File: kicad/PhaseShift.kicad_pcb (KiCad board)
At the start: 2 copper layers, 66.4 x 128.6 mm, 54 parts

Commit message: Silk Screen
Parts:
- added G***: LOGO, omnicode-9001:OmniCode-9001, F.Cu at (203.9, 150.6)
- added G***: LOGO, omnicode-9001:OmniCode-9001, B.Cu at (203.9, 150.7)
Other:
- board text added: "OmniCode:9001 - 202507.01"
- board text added: "OmniCode:9001 - PhaseShift"
- board text added: "PhaseShift"

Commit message: changed screw sizes
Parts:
- H1, H2, H3, H4, H5: value MountingHole_3.2mm_Pad -> MountingHole_2.2mm_M2_Pad; footprint TB2086_MISC:MountingHole_3.2mm_Pad -> TB2086_MISC:MountingHole_2.2mm_M2_Pad
- moved LED1 0.41 mm to (185.4, 101.9)
- moved R1 0.41 mm to (185.4, 101.9)
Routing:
- net Net-(LED1-K): track 4.27 -> 2.13 mm
- net +5V: track 318.8 -> 318.1 mm
- net ROW13: track 159.0 -> 158.4 mm
- net Net-(L11-DIN): track 15.0 -> 14.4 mm
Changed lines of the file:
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@@
 		)
 	)
-	(footprint "TB2086_MISC:MountingHole_3.2mm_Pad"
+	(footprint "TB2086_MISC:MountingHole_2.2mm_M2_Pad"
 		(layer "F.Cu")
 		(at 214.025 142.3875)
-		(descr "Mounting Hole 3.2mm, no annular, M3")
-		(tags "mounting hole 3.2mm no annular m3")
+		(descr "Mounting Hole 2.2mm, M2")
+		(tags "mounting hole 2.2mm m2")
 		(property "Reference" "H5"
-			(at 0 -4.2 0)
+			(at 0 -3.2 0)
 			(layer "F.SilkS")
 			(hide yes)
@@
 			)
 		)
-		(property "Value" "MountingHole_3.2mm_Pad"
-			(at 0 4.2 0)
+		(property "Value" "MountingHole_2.2mm_M2_Pad"
+			(at 0 3.2 0)
 			(layer "F.Fab")
 			(effects
@@
 		(fp_circle
 			(center 0 0)
-			(end 3.2 0)
+			(end 2.2 0)
 			(stroke
 				(width 0.15)
@@
 		(fp_circle
 			(center 0 0)
-			(end 3.45 0)
+			(end 2.45 0)
 			(stroke
 				(width 0.05)
@@
 		(pad "1" thru_hole circle
 			(at 0 0)
-			(size 3.5 3.5)
-			(drill 3.2)
+			(size 4.4 4.4)
+			(drill 2.2)
 			(layers "*.Cu" "*.Mask")
 			(remove_unused_layers no)
 			(net 1 "GND")
-			(zone_connect 2)
 		)
 		(embedded_fonts no)
@@
 		)
 	)
-	(footprint "TB2086_MISC:MountingHole_3.2mm_Pad"
+	(footprint "TB2086_MISC:MountingHole_2.2mm_M2_Pad"
 		(layer "F.Cu")
 		(at 233.675 200.3)
-		(descr "Mounting Hole 3.2mm, no annular, M3")
-		(tags "mounting hole 3.2mm no annular m3")
+		(descr "Mounting Hole 2.2mm, M2")
+		(tags "mounting hole 2.2mm m2")
 		(property "Reference" "H3"
-			(at 0 -4.2 0)
+			(at 0 -3.2 0)
 			(layer "F.SilkS")
 			(hide yes)
@@
 			)
 		)
-		(property "Value" "MountingHole_3.2mm_Pad"
-			(at 0 4.2 0)
+		(property "Value" "MountingHole_2.2mm_M2_Pad"
+			(at 0 3.2 0)
 			(layer "F.Fab")
 			(effects
@@
 		(fp_circle
 			(center 0 0)
-			(end 3.2 0)
+			(end 2.2 0)
 			(stroke
 				(width 0.15)
@@
 		(fp_circle
 			(center 0 0)
-			(end 3.45 0)
+			(end 2.45 0)
 			(stroke
 				(width 0.05)
@@
 		(pad "1" thru_hole circle
 			(at 0 0)
-			(size 3.5 3.5)
-			(drill 3.2)
+			(size 4.4 4.4)
+			(drill 2.2)
 			(layers "*.Cu" "*.Mask")
 			(remove_unused_layers no)
 			(net 1 "GND")
-			(zone_connect 2)
 		)
 		(embedded_fonts no)
@@
 		)
 	)
-	(footprint "TB2086_MISC:MountingHole_3.2mm_Pad"
+	(footprint "TB2086_MISC:MountingHole_2.2mm_M2_Pad"
 		(layer "F.Cu")
 		(at 175.325 79.7125)
-		(descr "Mounting Hole 3.2mm, no annular, M3")
-		(tags "mounting hole 3.2mm no annular m3")
+		(descr "Mounting Hole 2.2mm, M2")
+		(tags "mounting hole 2.2mm m2")
 		(property "Reference" "H1"
-			(at 0 -4.2 0)
+			(at 0 -3.2 0)
 			(layer "F.SilkS")
 			(hide yes)
@@
 			)
 		)
-		(property "Value" "MountingHole_3.2mm_Pad"
-			(at 0 4.2 0)
+		(property "Value" "MountingHole_2.2mm_M2_Pad"
+			(at 0 3.2 0)
 			(layer "F.Fab")
 			(effects
@@
 		(fp_circle
 			(center 0 0)
-			(end 3.2 0)
+			(end 2.2 0)
 			(stroke
 				(width 0.15)
@@
 		(fp_circle
 			(center 0 0)
-			(end 3.45 0)
+			(end 2.45 0)
 			(stroke
 				(width 0.05)
@@
 		(pad "1" thru_hole circle
 			(at 0 0)
-			(size 3.5 3.5)
-			(drill 3.2)
+			(size 4.4 4.4)
+			(drill 2.2)
 			(layers "*.Cu" "*.Mask")
 			(remove_unused_layers no)
 			(net 1 "GND")
-			(zone_connect 2)
 		)
 		(embedded_fonts no)
@@
 		)
 	)
-	(footprint "TB2086_MISC:MountingHole_3.2mm_Pad"
+	(footprint "TB2086_MISC:MountingHole_2.2mm_M2_Pad"
 		(layer "F.Cu")
 		(at 233.675 79.7125)
-		(descr "Mounting Hole 3.2mm, no annular, M3")
-		(tags "mounting hole 3.2mm no annular m3")
+		(descr "Mounting Hole 2.2mm, M2")
+		(tags "mounting hole 2.2mm m2")
 		(property "Reference" "H2"
-			(at 0 -4.2 0)
+			(at 0 -3.2 0)
 			(layer "F.SilkS")
 			(hide yes)
@@
 			)
 		)
-		(property "Value" "MountingHole_3.2mm_Pad"
-			(at 0 4.2 0)
+		(property "Value" "MountingHole_2.2mm_M2_Pad"
+			(at 0 3.2 0)
 			(layer "F.Fab")
 			(effects
@@
 		(fp_circle
 			(center 0 0)
-			(end 3.2 0)
+			(end 2.2 0)
 			(stroke
 				(width 0.15)
@@
 		(fp_circle
 			(center 0 0)
-			(end 3.45 0)
+			(end 2.45 0)
 			(stroke
 				(width 0.05)
@@
 		(pad "1" thru_hole circle
 			(at 0 0)
-			(size 3.5 3.5)
-			(drill 3.2)
+			(size 4.4 4.4)
+			(drill 2.2)
 			(layers "*.Cu" "*.Mask")
 			(remove_unused_layers no)
 			(net 1 "GND")
-			(zone_connect 2)
 		)
 		(embedded_fonts no)
@@
 		)
 	)
-	(footprint "TB2086_MISC:MountingHole_3.2mm_Pad"
+	(footprint "TB2086_MISC:MountingHole_2.2mm_M2_Pad"
 		(layer "F.Cu")
 		(at 175.325 200.3)
-		(descr "Mounting Hole 3.2mm, no annular, M3")
-		(tags "mounting hole 3.2mm no annular m3")
+		(descr "Mounting Hole 2.2mm, M2")
+		(tags "mounting hole 2.2mm m2")
 		(property "Reference" "H4"
-			(at 0 -4.2 0)
+			(at 0 -3.2 0)
 			(layer "F.SilkS")
 			(hide yes)
@@
 			)
 		)
-		(property "Value" "MountingHole_3.2mm_Pad"
-			(at 0 4.2 0)
+		(property "Value" "MountingHole_2.2mm_M2_Pad"
+			(at 0 3.2 0)
 			(layer "F.Fab")
 			(effects
@@
 		(fp_circle
 			(center 0 0)
-			(end 3.2 0)
+			(end 2.2 0)
 			(stroke
 				(width 0.15)
@@
 		(fp_circle
 			(center 0 0)
-			(end 3.45 0)
+			(end 2.45 0)
 			(stroke
 				(width 0.05)
@@
 		(pad "1" thru_hole circle
 			(at 0 0)
-			(size 3.5 3.5)
-			(drill 3.2)
+			(size 4.4 4.4)
+			(drill 2.2)
 			(layers "*.Cu" "*.Mask")
 			(remove_unused_layers no)
 			(net 1 "GND")
-			(zone_connect 2)
 		)
 		(embedded_fonts no)
@@
 	(footprint "LED_SMD:LED_0603_1608Metric_Pad1.05x0.95mm_HandSolder"
 		(layer "F.Cu")
-		(at 185.45 101.5 180)
+		(at 185.45 101.90625 180)
 		(descr "LED SMD 0603 (1608 Metric), square (rectangular) end terminal, IPC-7351 nominal, (Body size source: http://www.tortai-tech.com/upload/download/2011102023233369053.pdf), generated with kicad-footprint-generator")
 		(tags "LED handsolder")
@@
 	(footprint "Resistor_SMD:R_0603_1608Metric"
 		(layer "B.Cu")
-		(at 185.45 101.5)
+		(at 185.45 101.90625)
 		(descr "Resistor SMD 0603 (1608 Metric), square (rectangular) end terminal, IPC-7351 nominal, (Body size source: IPC-SM-782 page 72, https://www.pcb-3d.com/wordpress/wp-content/uploads/ipc-sm-782a_amendment_1_and_2.pdf), generated with kicad-footprint-generator")
 		(tags "resistor")
@@
 			(net 1 "GND")
 			(pintype "passive")
+			(zone_connect 2)
 		)
 		(pad "2" smd roundrect
@@
 	)
 	(segment
-		(start 175.45 176.92)
-		(end 175.89 177.36)
-		(width 0.2)
-		(layer "B.Cu")
-		(net 4)
-	)
-	(segment
 		(start 202.775 122.6908)
 		(end 202.775 122.8125)
@@
 	)
 	(segment
-		(start 226.822 128.6325)
-		(end 226.3 128.6325)
-		(width 0.5)
-		(layer "B.Cu")
-		(net 24)
-	)
-	(segment
 		(start 201.75 184.0825)
 		(end 202.049 183.7835)
@@
 	)
 	(segment
-		(start 182.5658 107.7483)
-		(end 182.7 107.8825)
-		(width 0.5)
-		(layer "B.Cu")
-		(net 24)
-	)
-	(segment
 		(start 202.049 183.121426)
 		(end 202.600426 182.57)
@@
 	)
 	(segment
-		(start 201.1525 185.7825)
-		(end 201.75 185.7825)
-		(width 0.2)
-		(layer "B.Cu")
-		(net 34)
-	)
-	(segment
 		(start 188.2 184.0825)
 		(end 189.0425 183.24)
@@
 	)
 	(segment
-		(start 184.575 101.5)
-		(end 176.0475 92.9725)
+		(start 184.575 101.90625)
+		(end 176.0475 93.37875)
 		(width 0.2)
 		(layer "F.Cu")
@@
 	)
 	(segment
-		(start 185.0857 99.8667)
-		(end 186.325 101.106)
+		(start 187.62625 101.90625)
+		(end 187.73 102.01)
 		(width 0.2)
 		(layer "F.Cu")
@@
 	)
 	(segment
-		(start 186.325 101.106)
-		(end 186.325 101.5)
+		(start 186.73125 101.90625)
+		(end 187.62625 101.90625)
 		(width 0.2)
 		(layer "F.Cu")
@@
 	)
 	(via
-		(at 185.0857 99.8667)
+		(at 187.73 102.01)
 		(size 0.8)
 		(drill 0.4)
@@
 	)
 	(segment
-		(start 186.275 101.5)
-		(end 185.0857 100.3107)
+		(start 187.62625 101.90625)
+		(end 187.73 102.01)
 		(width 0.2)
 		(layer "B.Cu")
@@
 	)
 	(segment
-		(start 185.0857 100.3107)
-		(end 185.0857 99.8667)
+		(start 186.68125 101.90625)
+		(end 187.62625 101.90625)
 		(width 0.2)
 		(layer "B.Cu")
@@
 		(width 0.2)
 		(layer "B.Cu")
-		(net 43)
-	)
-	(segment
-		(start 175.45 147.4675)
-		(end 175.6425 147.66)
-		(width 0.2)
-		(layer "B.Cu")

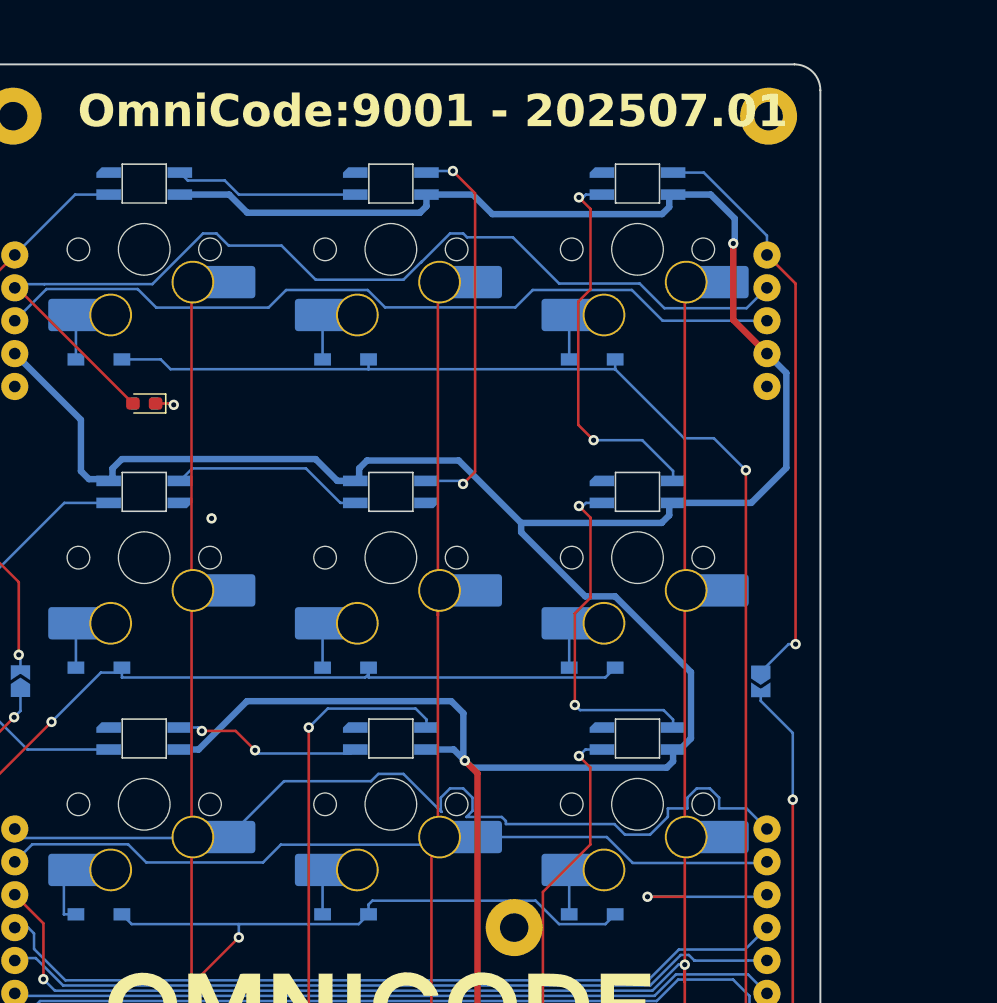
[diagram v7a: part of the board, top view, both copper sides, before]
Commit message: fixed positions for screw holes
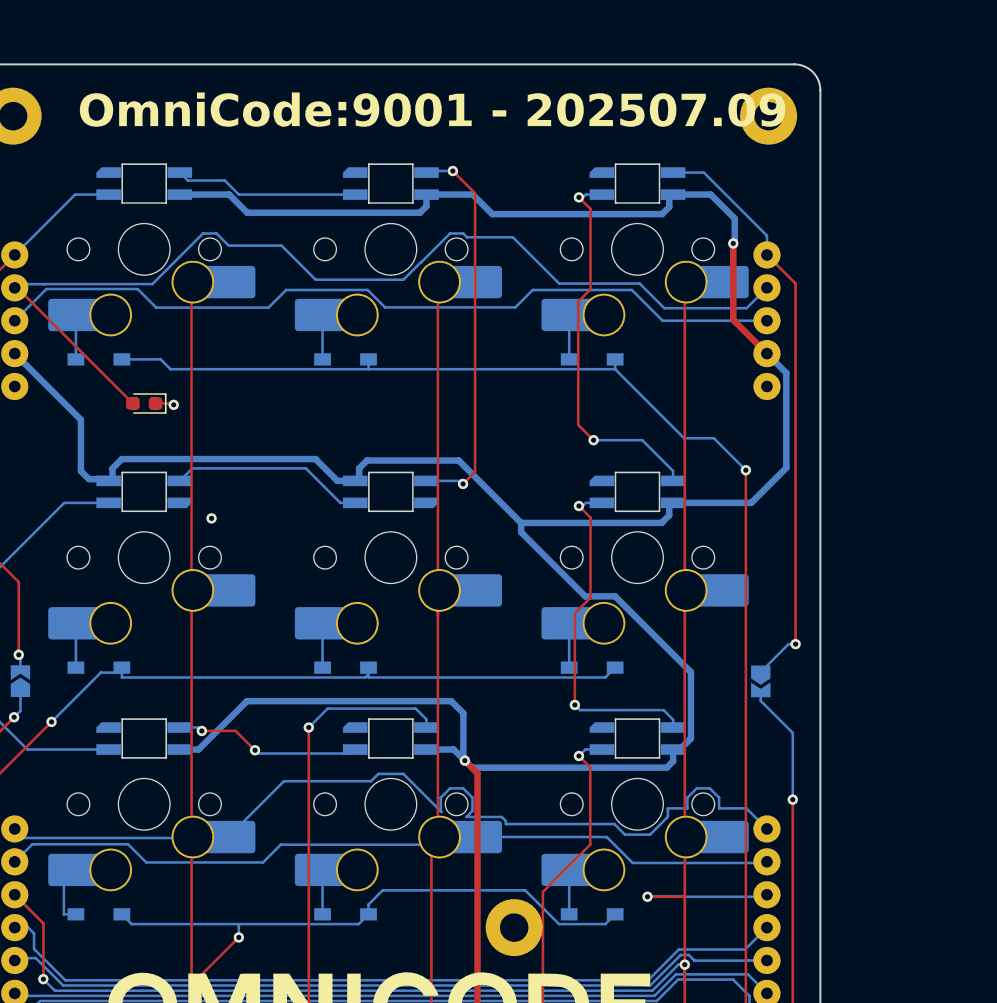
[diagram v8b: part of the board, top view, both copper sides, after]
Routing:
- net ROW14: track 137.1 -> 137.8 mm
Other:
- board text added: "OmniCode:9001 - 202507.09"
- board text removed: "OmniCode:9001 - 202507.01"
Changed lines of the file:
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@@
 		)
 	)
-	(gr_text "OmniCode:9001 - 202507.01"
+	(gr_text "OmniCode:9001 - 202507.09"
 		(at 180.31 80.79 0)
 		(layer "F.SilkS")
@@
 			(justify left bottom)
 		)
-		(render_cache "OmniCode:9001 - 202507.01" 0
+		(render_cache "OmniCode:9001 - 202507.09" 0
 			(polygon
 				(pts
@@
 			(polygon
 				(pts
-					(xy 225.536753 80.365) (xy 225.536753 80.091448) (xy 226.11744 80.091448) (xy 226.11744 78.066064)
-					(xy 225.561635 78.371978) (xy 225.495689 78.371978) (xy 225.495689 78.086519) (xy 226.213306 77.707637)
-					(xy 226.453427 77.707637) (xy 226.453427 80.091448) (xy 226.967405 80.091448) (xy 226.967405 80.365)
+					(xy 226.282498 77.690285) (xy 226.425442 77.724486) (xy 226.551128 77.779445) (xy 226.66219 77.855098)
+					(xy 226.760409 77.952796) (xy 226.858126 78.095255) (xy 226.930012 78.261304) (xy 226.975339 78.455318)
+					(xy 226.991372 78.682777) (xy 226.976305 78.919584) (xy 226.932019 79.141523) (xy 226.859086 79.350938)
+					(xy 226.757011 79.549821) (xy 226.624244 79.739738) (xy 226.367748 80.04051) (xy 226.163613 80.244987)
+					(xy 226.002646 80.374769) (xy 225.572626 80.374769) (xy 225.572626 80.259822) (xy 225.821129 80.10649)
+					(xy 226.046423 79.929154) (xy 226.250095 79.726915) (xy 226.433078 79.501853) (xy 226.551491 79.313449)
+					(xy 226.619207 79.155234) (xy 226.470613 79.26872) (xy 226.319551 79.345744) (xy 226.161845 79.392525)
+					(xy 226.011195 79.407568) (xy 225.846502 79.392584) (xy 225.703672 79.349598) (xy 225.578502 79.279674)
+					(xy 225.46806 79.181338) (xy 225.379604 79.062712) (xy 225.315583 78.927549) (xy 225.27577 78.772742)
+					(xy 225.261827 78.594239) (xy 225.262791 78.582332) (xy 225.602851 78.582332) (xy 225.613079 78.713774)
+					(xy 225.641635 78.822056) (xy 225.686516 78.911446) (xy 225.747412 78.98518) (xy 225.851072 79.06163)
+					(xy 225.972087 79.108044) (xy 226.115456 79.124246) (xy 226.25513 79.111059) (xy 226.387786 79.071734)
+					(xy 226.513861 79.010599) (xy 226.635235 78.930531) (xy 226.645921 78.784748) (xy 226.650195 78.630112)
+					(xy 226.639549 78.467882) (xy 226.609885 78.333438) (xy 226.563664 78.222094) (xy 226.50197 78.130025)
+					(xy 226.421724 78.051648) (xy 226.332041 77.996756) (xy 226.230958 77.963416) (xy 226.115456 77.95188)
+					(xy 226.003133 77.963094) (xy 225.905521 77.995406) (xy 225.819566 78.048461) (xy 225.743291 78.124071)
+					(xy 225.667736 78.245988) (xy 225.619992 78.39628) (xy 225.602851 78.582332) (xy 225.262791 78.582332)
+					(xy 225.276933 78.407706) (xy 225.320815 78.23966) (xy 225.392705 78.08678) (xy 225.493705 77.946537)
+					(xy 225.618567 77.830063) (xy 225.761698 77.747224) (xy 225.926727 77.696182) (xy 226.118967 77.678328)
 				)
 			)
 		)
 	)
-	(gr_text "OmniCode:9001 - 202507.01"
+	(gr_text "OmniCode:9001 - 202507.09"
 		(at 228.19 80.79 0)
 		(layer "B.SilkS")
@@
 			(justify left bottom mirror)
 		)
-		(render_cache "OmniCode:9001 - 202507.01" 0
+		(render_cache "OmniCode:9001 - 202507.09" 0
 			(polygon
 				(pts
@@
 			(polygon
 				(pts
-					(xy 182.963246 80.365) (xy 182.963246 80.091448) (xy 182.382559 80.091448) (xy 182.382559 78.066064)
-					(xy 182.938364 78.371978) (xy 183.00431 78.371978) (xy 183.00431 78.086519) (xy 182.286693 77.707637)
-					(xy 182.046572 77.707637) (xy 182.046572 80.091448) (xy 181.532594 80.091448) (xy 181.532594 80.365)
+					(xy 182.573272 77.696182) (xy 182.738301 77.747224) (xy 182.881432 77.830063) (xy 183.006294 77.946537)
+					(xy 183.107294 78.08678) (xy 183.179184 78.23966) (xy 183.223066 78.407706) (xy 183.238172 78.594239)
+					(xy 183.224229 78.772742) (xy 183.184416 78.927549) (xy 183.120395 79.062712) (xy 183.031939 79.181338)
+					(xy 182.921497 79.279674) (xy 182.796327 79.349598) (xy 182.653497 79.392584) (xy 182.488804 79.407568)
+					(xy 182.338154 79.392525) (xy 182.180448 79.345744) (xy 182.029386 79.26872) (xy 181.880792 79.155234)
+					(xy 181.948508 79.313449) (xy 182.066921 79.501853) (xy 182.249904 79.726915) (xy 182.453576 79.929154)
+					(xy 182.67887 80.10649) (xy 182.927373 80.259822) (xy 182.927373 80.374769) (xy 182.497353 80.374769)
+					(xy 182.336386 80.244987) (xy 182.132251 80.04051) (xy 181.875755 79.739738) (xy 181.742988 79.549821)
+					(xy 181.640913 79.350938) (xy 181.56798 79.141523) (xy 181.523694 78.919584) (xy 181.508627 78.682777)
+					(xy 181.512339 78.630112) (xy 181.849804 78.630112) (xy 181.854078 78.784748) (xy 181.864764 78.930531)
+					(xy 181.986138 79.010599) (xy 182.112213 79.071734) (xy 182.244869 79.111059) (xy 182.384543 79.124246)
+					(xy 182.527912 79.108044) (xy 182.648927 79.06163) (xy 182.752587 78.98518) (xy 182.813483 78.911446)
+					(xy 182.858364 78.822056) (xy 182.88692 78.713774) (xy 182.897148 78.582332) (xy 182.880007 78.39628)
+					(xy 182.832263 78.245988) (xy 182.756708 78.124071) (xy 182.680433 78.048461) (xy 182.594478 77.995406)
+					(xy 182.496866 77.963094) (xy 182.384543 77.95188) (xy 182.269041 77.963416) (xy 182.167958 77.996756)
+					(xy 182.078275 78.051648) (xy 181.998029 78.130025) (xy 181.936335 78.222094) (xy 181.890114 78.333438)
+					(xy 181.86045 78.467882) (xy 181.849804 78.630112) (xy 181.512339 78.630112) (xy 181.52466 78.455318)
+					(xy 181.569987 78.261304) (xy 181.641873 78.095255) (xy 181.73959 77.952796) (xy 181.837809 77.855098)
+					(xy 181.948871 77.779445) (xy 182.074557 77.724486) (xy 182.217501 77.690285) (xy 182.381032 77.678328)
 				)
 			)
@@
 	)
 	(segment
+		(start 202.775 140.6058)
+		(end 202.775 141.3625)
+		(width 0.2)
+		(layer "B.Cu")
+		(net 7)
+	)
+	(segment
+		(start 217.4917 142.1192)
+		(end 214.8825 139.51)
+		(width 0.2)
+		(layer "B.Cu")
+		(net 7)
+	)
+	(segment
+		(start 189.885 177.9)
+		(end 190.095 178.11)
+		(width 0.2)
+		(layer "B.Cu")
+		(net 7)
+	)
+	(segment
+		(start 175.8021 179.1079)
+		(end 177.01 177.9)
+		(width 0.2)
+		(layer "B.Cu")
+		(net 7)
+	)
+	(segment
+		(start 214.8825 139.51)
+		(end 203.8708 139.51)
+		(width 0.2)
+		(layer "B.Cu")
+		(net 7)
+	)
+	(segment
+		(start 192.7576 142.1192)
+		(end 192.7576 143.1483)
+		(width 0.2)
+		(layer "B.Cu")
+		(net 7)
+	)
+	(segment
+		(start 183.725 141.3625)
+		(end 184.4817 142.1192)
+		(width 0.2)
+		(layer "B.Cu")
+		(net 7)
+	)
+	(segment
+		(start 202.0183 142.1192)
+		(end 192.7576 142.1192)
+		(width 0.2)
+		(layer "B.Cu")
+		(net 7)
+	)
+	(segment
+		(start 184.4817 142.1192)
+		(end 192.7576 142.1192)
+		(width 0.2)
+		(layer "B.Cu")
+		(net 7)
+	)
+	(segment
+		(start 221.0683 142.1192)
+		(end 217.4917 142.1192)
+		(width 0.2)
+		(layer "B.Cu")
+		(net 7)
+	)
+	(segment
+		(start 233.55 179.46)
+		(end 232.7431 178.6531)
+		(width 0.2)
+		(layer "B.Cu")
+		(net 7)
+	)
+	(segment
+		(start 203.8708 139.51)
+		(end 202.775 140.6058)
+		(width 0.2)
+		(layer "B.Cu")
+		(net 7)
+	)
+	(segment
 		(start 221.825 141.3625)
 		(end 221.0683 142.1192)
 		(width 0.2)
 		(layer "B.Cu")
-		(net 7)
-	)
-	(segment
-		(start 189.885 177.9)
-		(end 190.095 178.11)
-		(width 0.2)
-		(layer "B.Cu")
-		(net 7)
-	)
-	(segment
-		(start 175.8021 179.1079)
-		(end 177.01 177.9)
-		(width 0.2)
-		(layer "B.Cu")
-		(net 7)
-	)
-	(segment
-		(start 192.7576 142.1192)
-		(end 192.7576 143.1483)
-		(width 0.2)
-		(layer "B.Cu")
-		(net 7)
-	)
-	(segment
-		(start 183.725 141.3625)
-		(end 184.4817 142.1192)
-		(width 0.2)
-		(layer "B.Cu")
-		(net 7)
-	)
-	(segment
-		(start 203.0731 140.3077)
-		(end 202.775 140.6058)
-		(width 0.2)
-		(layer "B.Cu")
-		(net 7)
-	)
-	(segment
-		(start 202.0183 142.1192)
-		(end 192.7576 142.1192)
-		(width 0.2)
-		(layer "B.Cu")
-		(net 7)
-	)
-	(segment
-		(start 215.6802 140.3077)
-		(end 203.0731 140.3077)
-		(width 0.2)
-		(layer "B.Cu")
-		(net 7)
-	)
-	(segment
-		(start 221.0683 142.1192)
-		(end 217.4917 142.1192)
-		(width 0.2)
-		(layer "B.Cu")
-		(net 7)
-	)
-	(segment
-		(start 184.4817 142.1192)
-		(end 192.7576 142.1192)
-		(width 0.2)
-		(layer "B.Cu")
-		(net 7)
-	)
-	(segment
-		(start 233.55 179.46)
-		(end 232.7431 178.6531)
-		(width 0.2)
-		(layer "B.Cu")
-		(net 7)
-	)
-	(segment
-		(start 217.4917 142.1192)
-		(end 215.6802 140.3077)
-		(width 0.2)
-		(layer "B.Cu")
-		(net 7)
-	)
-	(segment
-		(start 202.775 140.6058)
-		(end 202.775 141.3625)
-		(width 0.2)
-		(layer "B.Cu")
